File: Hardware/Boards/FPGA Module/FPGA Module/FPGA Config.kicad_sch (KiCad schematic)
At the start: 13 parts, among them U1 XCKU3P-FFVA676, U19 MAX6070BAUT12V+T

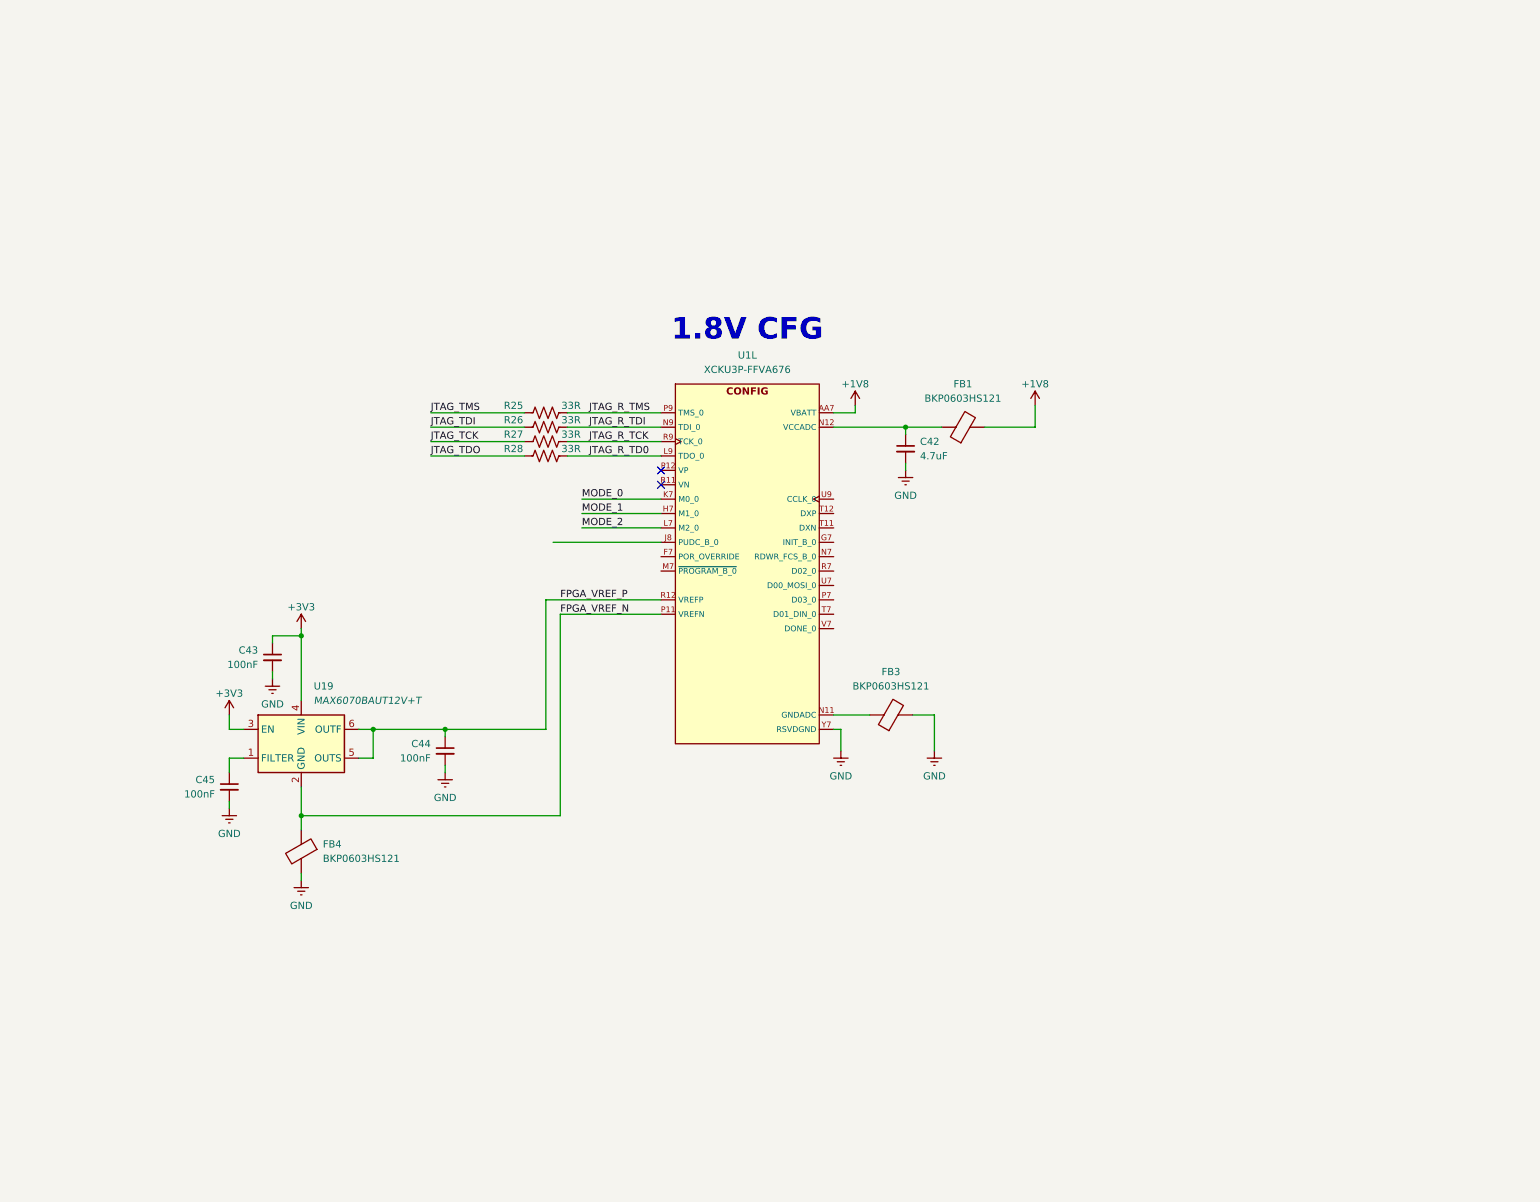
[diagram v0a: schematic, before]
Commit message: Using new DP to HDMI IC
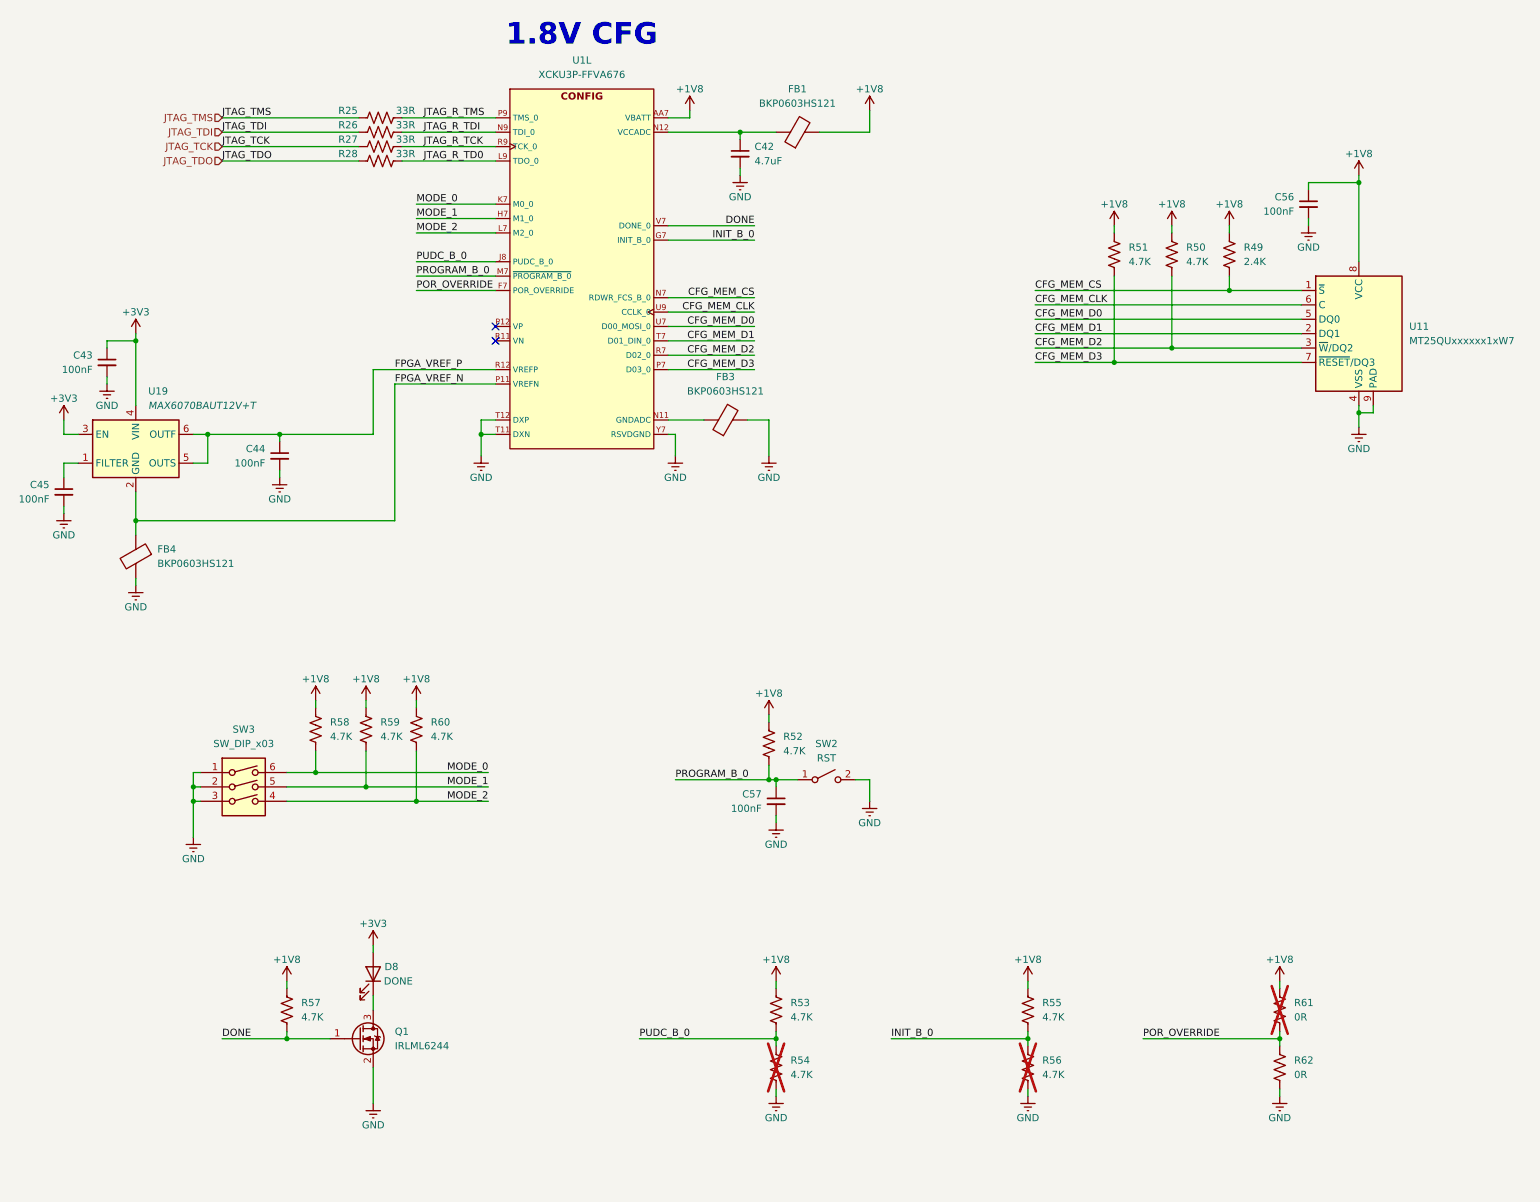
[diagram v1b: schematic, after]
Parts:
- added C56, C57: 100nF, Capacitor_SMD:C_0402_1005Metric, symbol Device:C_Small
- added D8: DONE, LED_SMD:LED_0603_1608Metric, symbol Device:LED
- added Q1: IRLML6244, Package_TO_SOT_SMD:SOT-23, symbol Transistor_FET:IRLML6244
- added R49: 2.4K, Resistor_SMD:R_0402_1005Metric, symbol Device:R_US
- added R50, R51, R52, R53, R54, R55, R56, R57, R58, R59, R60: 4.7K, Resistor_SMD:R_0402_1005Metric, symbol Device:R_US
- added R61, R62: 0R, Resistor_SMD:R_0402_1005Metric, symbol Device:R_US
- added SW2: RST, Button_Switch_SMD:SW_Push_SPST_NO_Alps_SKRK, symbol Switch:SW_SPST
- added SW3: SW_DIP_x03, Button_Switch_SMD:SW_DIP_SPSTx03_Slide_KingTek_DSHP03TJ_W5.25mm_P1.27mm_JPin, symbol Switch:SW_DIP_x03
- added U11: MT25QUxxxxxx1xW7, Package_DFN_QFN:W-PDFN-8-1EP_6x5mm_P1.27mm_EP3x3mm, symbol Memory_Flash:MT25QUxxxxxx1xW7
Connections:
- net +1V8: now also C56.1, R49.2, R50.2, R51.2, R52.2, R53.2, R55.2, R57.2, R58.2, R59.2, R60.2, R61.2, U11.8 (VCC)
- net +3V3: now also D8.2 (A)
- net GND: now also U1.T11 (DXN), U1.T12 (DXP), C56.2, C57.2, Q1.2 (S), R54.1, R56.1, R62.1, SW2.2 (B), SW3.1, SW3.2, SW3.3, U11.4 (VSS), U11.9 (PAD)
- net MODE_0: now also R58.1, SW3.6
- net MODE_1: now also R59.1, SW3.5
- net MODE_2: now also R60.1, SW3.4
- net POR_OVERRIDE: now reaches U1.F7 (POR_OVERRIDE)
- net POR_OVERRIDE: now also R61.1, R62.2
- net INIT_B_0: now reaches U1.G7 (INIT_B_0)
- net INIT_B_0: now also R55.1, R56.2
- net PUDC_B_0: now reaches U1.J8 (PUDC_B_0)
- net PUDC_B_0: now also R53.1, R54.2
- net PROGRAM_B_0: now reaches U1.M7 (~{PROGRAM_B_0})
- net PROGRAM_B_0: now also C57.1, R52.1, SW2.1 (A)
- net CFG_MEM_CS: now reaches U1.N7 (RDWR_FCS_B_0)
- net CFG_MEM_CS: now also R49.1, U11.1 (~{S})
- net CFG_MEM_D3: now reaches U1.P7 (D03_0)
- net CFG_MEM_D3: now also R51.1, U11.7 (~{RESET}/DQ3)
- net CFG_MEM_D2: now reaches U1.R7 (D02_0)
- net CFG_MEM_D2: now also R50.1, U11.3 (~{W}/DQ2)
- net CFG_MEM_D1: now reaches U1.T7 (D01_DIN_0)
- net CFG_MEM_D1: now also U11.2 (DQ1)
- net CFG_MEM_D0: now reaches U1.U7 (D00_MOSI_0)
- net CFG_MEM_D0: now also U11.5 (DQ0)
- net CFG_MEM_CLK: now reaches U1.U9 (CCLK_0)
- net CFG_MEM_CLK: now also U11.6 (C)
- net DONE: now reaches U1.V7 (DONE_0)
- net DONE: now also Q1.1 (G), R57.1
- new net: D8.1 (K), Q1.3 (D)
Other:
- moved on the sheet: C42, C43, C44, C45, FB1, FB3, FB4, R25, R26, R27, R28, U19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

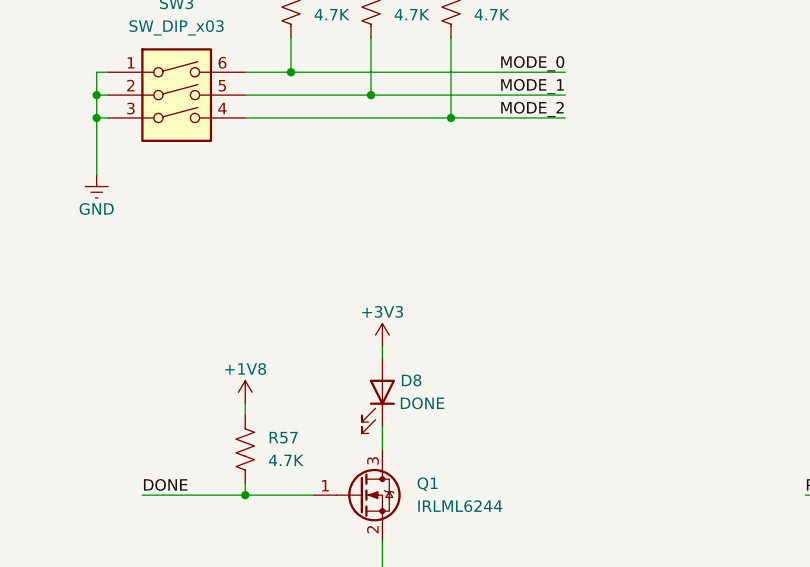
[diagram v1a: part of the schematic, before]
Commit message: updated fpga module schematics
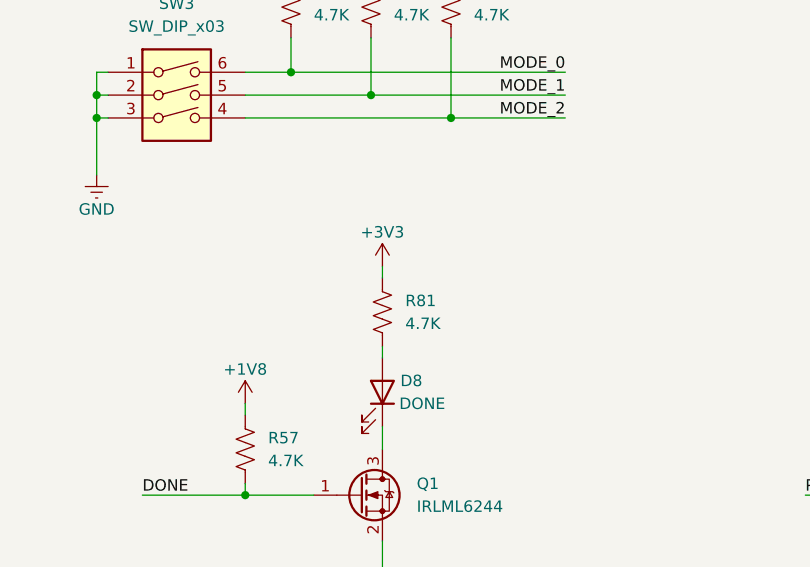
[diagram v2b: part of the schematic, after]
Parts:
- added R81: 4.7K, Resistor_SMD:R_0402_1005Metric, symbol Device:R_US
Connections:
- net +3V3: now also R81.2; no longer D8.2 (A)
- new net: D8.2 (A), R81.1
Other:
- company: (none) -> Drexel University
- title: (none) -> FPGA Configuration
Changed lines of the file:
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@@
 	(generator_version "8.0")
 	(paper "A3")
+	(title_block
+		(title "FPGA Configuration")
+		(date "2024-07-31")
+		(rev "1.0")
+		(company "Drexel University")
+		(comment 1 "Designed by John Hofmeyr")
+	)
 	(junction
 		(at 102.87 177.8)
@@
 	(wire
 		(pts
+			(xy 134.62 194.31) (xy 134.62 195.58)
+		)
+		(stroke
+			(width 0)
+			(type default)
+		)
+	)
+	(wire
+		(pts
 			(xy 92.71 96.52) (xy 92.71 107.95)
 		)
@@
 	(wire
 		(pts
-			(xy 134.62 203.2) (xy 134.62 204.47)
-		)
-		(stroke
-			(width 0)
-			(type default)
-		)
-	)
-	(wire
-		(pts
 			(xy 107.95 219.71) (xy 119.38 219.71)
 		)
@@
 	(wire
 		(pts
+			(xy 134.62 203.2) (xy 134.62 204.47)
+		)
+		(stroke
+			(width 0)
+			(type default)
+		)
+	)
+	(wire
+		(pts
 			(xy 142.24 160.02) (xy 142.24 161.29)
 		)
@@
 	(symbol
 		(lib_id "power:+3V3")
-		(at 134.62 203.2 0)
+		(at 134.62 194.31 0)
 		(unit 1)
 		(exclude_from_sim no)
@@
 		(dnp no)
 		(property "Reference" "#PWR0176"
-			(at 134.62 207.01 0)
+			(at 134.62 198.12 0)
 			(effects
 				(font
@@
 		)
 		(property "Value" "+3V3"
-			(at 134.62 199.39 0)
+			(at 134.62 190.5 0)
 			(effects
 				(font
@@
 		)
 		(property "Footprint" ""
-			(at 134.62 203.2 0)
+			(at 134.62 194.31 0)
 			(effects
 				(font
@@
 		)
 		(property "Datasheet" ""
-			(at 134.62 203.2 0)
+			(at 134.62 194.31 0)
 			(effects
 				(font
@@
 		)
 		(property "Description" "Power symbol creates a global label with name \"+3V3\""
-			(at 134.62 203.2 0)
+			(at 134.62 194.31 0)
 			(effects
 				(font
@@
 					(unit 1)
 				)
+			)
+		)
+	)
+	(symbol
+		(lib_id "Device:R_US")
+		(at 134.62 199.39 180)
+		(unit 1)
+		(exclude_from_sim no)
+		(in_bom yes)
+		(on_board yes)
+		(dnp no)
+		(fields_autoplaced yes)
+		(property "Reference" "R81"
+			(at 137.16 198.1199 0)
+			(effects
+				(font
+					(size 1.27 1.27)
+				)
+				(justify right)
+			)
+		)
+		(property "Value" "4.7K"
+			(at 137.16 200.6599 0)
+			(effects
+				(font
+					(size 1.27 1.27)
+				)
+				(justify right)
+			)
+		)
+		(property "Footprint" "Resistor_SMD:R_0402_1005Metric"
+			(at 133.604 199.136 90)
+			(effects
+				(font
+					(size 1.27 1.27)
+				)
+				(hide yes)
+			)
+		)
+		(property "Datasheet" "~"
+			(at 134.62 199.39 0)
+			(effects
+				(font
+					(size 1.27 1.27)
+				)
+				(hide yes)
+			)
+		)
+		(property "Description" "Resistor, US symbol"
+			(at 134.62 199.39 0)
+			(effects
+				(font
+					(size 1.27 1.27)
+				)
+				(hide yes)
+			)
+		)
+		(pin "1"
+		)
+		(pin "2"
+		)
+		(instances
+			(project "FPGA Module"
+				(path "/199f10e2-d4b4-4a27-9e84-7b1ce2ae6bf0/0c296310-f788-47f0-8a3f-43c3444563e8/2e9d2356-e08c-4cea-be34-327b495582c0"
+					(reference "R81")
+					(unit 1)
+				)

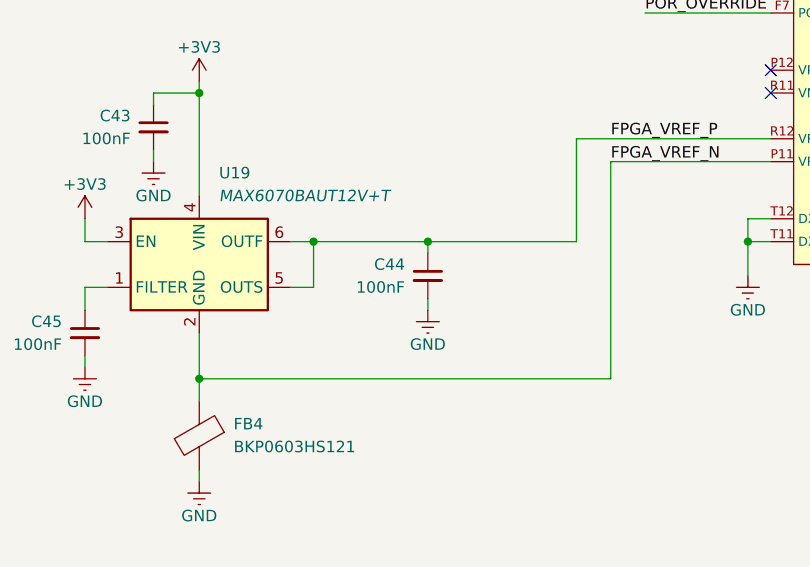
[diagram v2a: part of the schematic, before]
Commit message: FPGA Module sch update
Added 3V3 LDO for MCU and 3V3 EN for DCDC. Also added SPI bus from MCU to FPGA with level shifter
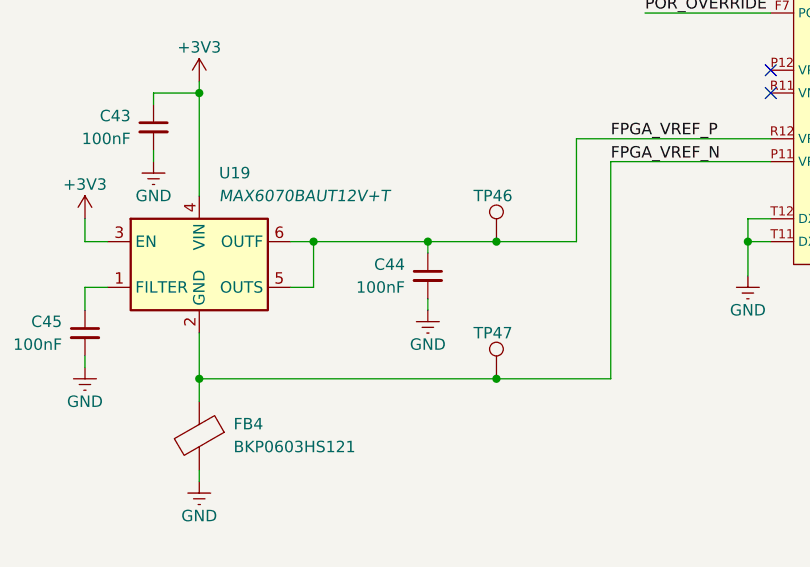
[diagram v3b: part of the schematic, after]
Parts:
- added TP46, TP47: Test Point, FPGA Module:Test Point 0.75mm, symbol Connector:TestPoint
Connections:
- net FPGA_VREF_N: now also TP47.1
- net FPGA_VREF_P: now also TP46.1
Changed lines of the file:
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@@
 	)
 	(junction
+		(at 125.73 128.27)
+		(diameter 0)
+		(color 0 0 0 0)
+	)
+	(junction
 		(at 205.74 219.71)
 		(diameter 0)
@@
 	)
 	(junction
+		(at 125.73 113.03)
+		(diameter 0)
+		(color 0 0 0 0)
+	)
+	(junction
 		(at 199.39 59.69)
 		(diameter 0)
@@
 	(wire
 		(pts
+			(xy 125.73 128.27) (xy 92.71 128.27)
+		)
+		(stroke
+			(width 0)
+			(type default)
+		)
+	)
+	(wire
+		(pts
 			(xy 265.43 100.33) (xy 298.45 100.33)
 		)
@@
 	(wire
 		(pts
+			(xy 125.73 113.03) (xy 118.11 113.03)
+		)
+		(stroke
+			(width 0)
+			(type default)
+		)
+	)
+	(wire
+		(pts
 			(xy 133.35 168.91) (xy 133.35 175.26)
 		)
@@
 	(wire
 		(pts
-			(xy 134.62 113.03) (xy 118.11 113.03)
+			(xy 134.62 113.03) (xy 125.73 113.03)
 		)
 		(stroke
@@
 	(wire
 		(pts
-			(xy 138.43 128.27) (xy 92.71 128.27)
+			(xy 138.43 128.27) (xy 125.73 128.27)
 		)
 		(stroke
@@
 	)
 	(symbol
+		(lib_id "Connector:TestPoint")
+		(at 125.73 113.03 0)
+		(unit 1)
+		(exclude_from_sim no)
+		(in_bom yes)
+		(on_board yes)
+		(dnp no)
+		(property "Reference" "TP46"
+			(at 123.19 107.95 0)
+			(effects
+				(font
+					(size 1.27 1.27)
+				)
+				(justify left)
+			)
+		)
+		(property "Value" "Test Point"
+			(at 120.65 107.315 0)
+			(effects
+				(font
+					(size 1.27 1.27)
+				)
+				(justify left)
+				(hide yes)
+			)
+		)
+		(property "Footprint" "FPGA Module:Test Point 0.75mm"
+			(at 130.81 113.03 0)
+			(effects
+				(font
+					(size 1.27 1.27)
+				)
+				(hide yes)
+			)
+		)
+		(property "Datasheet" "~"
+			(at 130.81 113.03 0)
+			(effects
+				(font
+					(size 1.27 1.27)
+				)
+				(hide yes)
+			)
+		)
+		(property "Description" "test point"
+			(at 125.73 113.03 0)
+			(effects
+				(font
+					(size 1.27 1.27)
+				)
+				(hide yes)
+			)
+		)
+		(pin "1"
+		)
+		(instances
+			(project "FPGA Module"
+				(path "/199f10e2-d4b4-4a27-9e84-7b1ce2ae6bf0/0c296310-f788-47f0-8a3f-43c3444563e8/2e9d2356-e08c-4cea-be34-327b495582c0"
+					(reference "TP46")
+					(unit 1)
+				)
+			)
+		)
+	)
+	(symbol
 		(lib_id "Device:R_US")
 		(at 205.74 224.79 180)
@@
 					(unit 1)
 				)
+			)
+		)
+	)
+	(symbol
+		(lib_id "Connector:TestPoint")
+		(at 125.73 128.27 0)
+		(unit 1)
+		(exclude_from_sim no)
+		(in_bom yes)
+		(on_board yes)
+		(dnp no)
+		(property "Reference" "TP47"
+			(at 123.19 123.19 0)
+			(effects
+				(font
+					(size 1.27 1.27)
+				)
+				(justify left)
+			)
+		)
+		(property "Value" "Test Point"
+			(at 120.65 122.555 0)
+			(effects
+				(font
+					(size 1.27 1.27)
+				)
+				(justify left)
+				(hide yes)
+			)
+		)
+		(property "Footprint" "FPGA Module:Test Point 0.75mm"
+			(at 130.81 128.27 0)
+			(effects
+				(font
+					(size 1.27 1.27)
+				)
+				(hide yes)
+			)
+		)
+		(property "Datasheet" "~"
+			(at 130.81 128.27 0)
+			(effects
+				(font
+					(size 1.27 1.27)
+				)
+				(hide yes)
+			)
+		)
+		(property "Description" "test point"
+			(at 125.73 128.27 0)
+			(effects
+				(font
+					(size 1.27 1.27)
+				)
+				(hide yes)
+			)
+		)
+		(pin "1"
+		)
+		(instances
+			(project "FPGA Module"
+				(path "/199f10e2-d4b4-4a27-9e84-7b1ce2ae6bf0/0c296310-f788-47f0-8a3f-43c3444563e8/2e9d2356-e08c-4cea-be34-327b495582c0"
+					(reference "TP47")
+					(unit 1)
+				)
